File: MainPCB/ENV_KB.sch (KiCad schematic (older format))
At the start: 197 parts, among them J0 TYPE-C-31-M-12

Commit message: Changed Button to B3U from EVQ + smaller LED resistor
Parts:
- PowerLED0: value Green Power Led -> LED 0805
- PowerLedResistor0: value 1K Resistor -> 1K Resistor 0402; footprint Resistor_SMD:R_0805_2012Metric -> Resistor_SMD:R_0402_1005Metric
- RESISTOR0, RESISTOR1: value 5.1kohm -> 5.1kohm 0402
- SW-RST0: value Reset Buton -> B3U-1000; footprint Button_Switch_SMD:Panasonic_EVQPUJ_EVQPUA -> Button_Switch_SMD:SW_SPST_B3U-1000P; symbol Switch:SW_Push_Dual -> Switch:SW_Push
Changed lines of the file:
@@
 P 9950 8950
 F 0 "RESISTOR1" V 9754 8950 39  0001 C CNN
-F 1 "5.1kohm" V 10050 8950 30  0000 C CNN
+F 1 "5.1kohm 0402" V 10050 8950 30  0000 C CNN
 F 2 "Resistor_SMD:R_0402_1005Metric" H 9950 8950 50  0001 C CNN
 F 3 "~" H 9950 8950 50  0001 C CNN
@@
 P 8350 8650
 F 0 "RESISTOR0" V 8154 8650 39  0001 C CNN
-F 1 "5.1kohm" V 8245 8650 50  0001 C CNN
+F 1 "5.1kohm 0402" V 8245 8650 50  0001 C CNN
 F 2 "Resistor_SMD:R_0402_1005Metric" H 8350 8650 50  0001 C CNN
 F 3 "~" H 8350 8650 50  0001 C CNN
@@
 P 8300 9950
 F 0 "PowerLED0" H 8293 10167 50  0001 C CNN
-F 1 "Green Power Led" H 8300 10050 50  0000 C CNN
+F 1 "LED 0805" H 8300 10050 50  0000 C CNN
 F 2 "LED_SMD:LED_0805_2012Metric_Castellated" H 8300 9950 50  0001 C CNN
 F 3 "~" H 8300 9950 50  0001 C CNN
@@
 P 8550 9950
 F 0 "PowerLedResistor0" V 8650 10200 50  0000 C CNN
-F 1 "1K Resistor" V 8700 10000 50  0001 C CNN
-F 2 "Resistor_SMD:R_0805_2012Metric" H 8550 9950 50  0001 C CNN
+F 1 "1K Resistor 0402" V 8700 10000 50  0001 C CNN
+F 2 "Resistor_SMD:R_0402_1005Metric" H 8550 9950 50  0001 C CNN
 F 3 "~" H 8550 9950 50  0001 C CNN
 F 4 "C17513" V 8550 9950 50  0001 C CNN "LSCS Part"
@@
 Resetbtn
 $Comp
-L Switch:SW_Push_Dual SW-RST0
+L Switch:SW_Push SW-RST0
 U 1 1 605FBFA6
 P 8550 10700
 F 0 "SW-RST0" H 8550 11100 50  0000 C CNN
-F 1 "Reset Buton" H 8550 10950 50  0000 C CNN
-F 2 "Button_Switch_SMD:Panasonic_EVQPUJ_EVQPUA" H 8550 10700 50  0001 L BNN
+F 1 "B3U-1000" H 8550 10950 50  0000 C CNN
+F 2 "Button_Switch_SMD:SW_SPST_B3U-1000P" H 8550 10700 50  0001 L BNN
 F 3 "" H 8550 10700 50  0001 L BNN
 F 4 "Omron" H 8550 10700 50  0001 L BNN "MANUFACTURER"
@@
 Text GLabel 8750 10700 2    50   Input ~ 0
 GND
-Text GLabel 8750 10900 2    50   Input ~ 0
-GND
-Text GLabel 8350 10900 0    50   Input ~ 0
-Resetbtn
 $Comp
 L Mechanical:MountingHole H7

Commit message: Re aligned all diodes and re-did traces for all diodes
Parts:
- removed H8: MountingHole, MountingHole:MountingHole_3.2mm_M3, symbol Mechanical:MountingHole
- D0, D1, D10, D11, D12, D13, D14, D15, D16, D17, D18, D19, D2, D20, D21, D22, D23, D24, D25, D26, D27, D28, D29, D3, D30, D31, D32, D33, D34, D35, D36, D37, D38, D39, D4, D40, D41, D42, D43, D44, D45, D46, D47, D48, D49, D5, D50, D51, D52, D53, D54, D55, D56, D57, D58, D59, D6, D60, D61, D62, D63, D64, D65, D66, D67, D68, D69, D7, D70, D71, D72, D73, D74, D75, D76, D77, D78, D79, D8, D80, D81, D82, D83, D84, D85, D86, D87, D88, D9: footprint CFTKB Bits:D_DO-35_SOD27_P5.08mm_Horizontal -> Diode_THT:D_DO-35_SOD27_P7.62mm_Horizontal
- J0: LCSC (none) -> C165948; LSCS Part C165948 -> (none)
- PowerLED0: value LED 0805 -> LED 0402; footprint LED_SMD:LED_0805_2012Metric_Castellated -> LED_SMD:LED_0402_1005Metric; LSCS Part C2297 -> (none)
- PowerLedResistor0: LCSC (none) -> C17513; LSCS Part C17513 -> (none)
- RESISTOR0, RESISTOR1: LCSC (none) -> C25905; LSCS Part C25905 -> (none)
- SW-RST0: LCSC (none) -> C231329

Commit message: changed type-c port and re-did some bits
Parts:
- removed J0: TYPE-C-31-M-12, EM_Extras:USB_C_Receptacle_HRO_TYPE-C-31-M-12, symbol Type-C-Lib:TYPE-C-31-M-12
- added USB1: HRO-TYPE-C-31-M-12, HRO-TYPE-C31-M-12:HRO-TYPE-C-31-M-12, symbol Type-C:HRO-TYPE-C-31-M-12
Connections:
- net labels added: VBUS
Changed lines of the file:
@@
 Text GLabel 12950 8900 1    50   Input ~ 0
 USB2_N
-Text GLabel 8450 8850 0    50   Input ~ 0
+Text GLabel 9300 8700 1    50   Input ~ 0
 USB2_N
-Text GLabel 9850 8850 2    50   Input ~ 0
+Text GLabel 9400 8700 1    50   Input ~ 0
 USB2_P
 Text GLabel 13100 8900 1    50   Input ~ 0
@@
 Text GLabel 13650 9100 2    50   Input ~ 0
 USBVBUS
-Text GLabel 9850 8450 2    50   Input ~ 0
+Text GLabel 8800 8700 1    50   Input ~ 0
 USBVBUS
-Text GLabel 10050 8950 2    50   Input ~ 0
+Text GLabel 9000 8500 1    50   Input ~ 0
 GND
 Text GLabel 12150 9300 0    50   Input ~ 0
@@
 L Device:R_Small RESISTOR1
 U 1 1 606333E5
-P 9950 8950
-F 0 "RESISTOR1" V 9754 8950 39  0001 C CNN
-F 1 "5.1kohm 0402" V 10050 8950 30  0000 C CNN
-F 2 "Resistor_SMD:R_0402_1005Metric" H 9950 8950 50  0001 C CNN
-F 3 "~" H 9950 8950 50  0001 C CNN
-F 4 "C25905" V 9950 8950 50  0001 C CNN "LCSC"
-	1    9950 8950
-	0    1    1    0
+P 9000 8600
+F 0 "RESISTOR1" V 8804 8600 39  0001 C CNN
+F 1 "5.1kohm 0402" V 9000 8700 30  0001 C CNN
+F 2 "Resistor_SMD:R_0402_1005Metric" H 9000 8600 50  0001 C CNN
+F 3 "~" H 9000 8600 50  0001 C CNN
+F 4 "C25905" V 9000 8600 50  0001 C CNN "LCSC"
+	1    9000 8600
+	1    0    0    -1
 $EndComp
 $Comp
 L Device:R_Small RESISTOR0
 U 1 1 6066AF89
-P 8350 8650
-F 0 "RESISTOR0" V 8154 8650 39  0001 C CNN
-F 1 "5.1kohm 0402" V 8245 8650 50  0001 C CNN
-F 2 "Resistor_SMD:R_0402_1005Metric" H 8350 8650 50  0001 C CNN
-F 3 "~" H 8350 8650 50  0001 C CNN
-F 4 "C25905" V 8350 8650 50  0001 C CNN "LCSC"
-	1    8350 8650
-	0    -1   -1   0
-$EndComp
-Text GLabel 8250 8650 0    50   Input ~ 0
-GND
-Text GLabel 9850 9150 2    50   Input ~ 0
-GND
-Text GLabel 9850 9250 2    50   Input ~ 0
-GND
-Text GLabel 9850 8750 2    50   Input ~ 0
+P 9600 8600
+F 0 "RESISTOR0" V 9404 8600 39  0001 C CNN
+F 1 "5.1kohm 0402" V 9495 8600 50  0001 C CNN
+F 2 "Resistor_SMD:R_0402_1005Metric" H 9600 8600 50  0001 C CNN
+F 3 "~" H 9600 8600 50  0001 C CNN
+F 4 "C25905" V 9600 8600 50  0001 C CNN "LCSC"
+	1    9600 8600
+	-1   0    0    1
+$EndComp
+Text GLabel 9600 8500 1    50   Input ~ 0
+GND
+Text GLabel 9800 8700 1    50   Input ~ 0
+GND
+Text GLabel 9900 8700 1    50   Input ~ 0
+GND
+Text GLabel 9100 8700 1    50   Input ~ 0
 USB2_N
-Text GLabel 8450 8750 0    50   Input ~ 0
+Text GLabel 9200 8700 1    50   Input ~ 0
 USB2_P
 $Comp
@@
 	0    1    1    0
 $EndComp
-$Comp
-L Type-C-Lib:TYPE-C-31-M-12 J0
-U 1 1 607F5ECC
-P 9150 8850
-F 0 "J0" H 9150 9517 50  0000 C CNN
-F 1 "TYPE-C-31-M-12" H 9150 9426 50  0000 C CNN
-F 2 "EM_Extras:USB_C_Receptacle_HRO_TYPE-C-31-M-12" H 9150 8250 50  0000 C CNN
-F 3 "~" H 9300 8850 50  0001 C CNN
-F 4 "HRO Electronics" H 9150 8850 50  0001 C CNN "MANUFACTURER"
-F 5 "3.31mm" H 9150 8850 50  0001 C CNN "MAXIMUM_PACKAGE_HEIGHT"
-F 6 "A" H 9150 8850 50  0001 C CNN "PARTREV"
-F 7 "Manufacturer Recommendations" H 9150 8850 50  0001 C CNN "STANDARD"
-F 8 "C165948" H 9150 8850 50  0001 C CNN "LCSC"
-	1    9150 8850
-	1    0    0    -1
-$EndComp
-Text GLabel 9850 9350 2    50   Input ~ 0
+Text GLabel 8700 8700 1    50   Input ~ 0
 GND
 $Comp
@@
 	1    0    0    -1
 $EndComp
+$Comp
+L Type-C:HRO-TYPE-C-31-M-12 USB1
+U 1 1 60AC4D40
+P 9250 8800
+F 0 "USB1" V 8650 9250 60  0000 C CNN
+F 1 "HRO-TYPE-C-31-M-12" V 8750 8800 60  0000 C CNN
+F 2 "HRO-TYPE-C31-M-12:HRO-TYPE-C-31-M-12" H 9250 8800 60  0001 C CNN
+F 3 "" H 9250 8800 60  0001 C CNN
+F 4 "C165948" H 9250 8800 50  0001 C CNN "LCSC"
+	1    9250 8800
+	0    -1   -1   0
+$EndComp
+Text GLabel 9700 8700 1    50   Input ~ 0
+VBUS
 $EndSCHEMATC

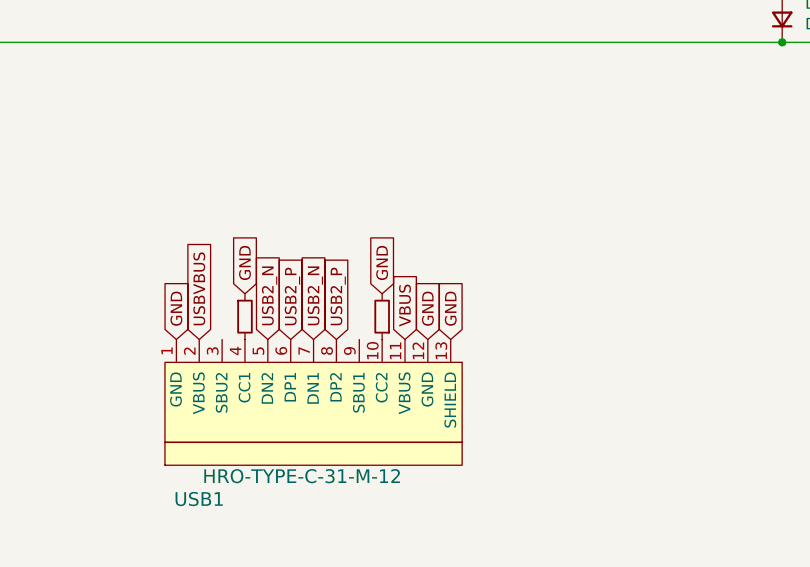
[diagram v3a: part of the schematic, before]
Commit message: adjusted traces, placements and clearances on main PCB and re-generated Gerber, Bom and Position file
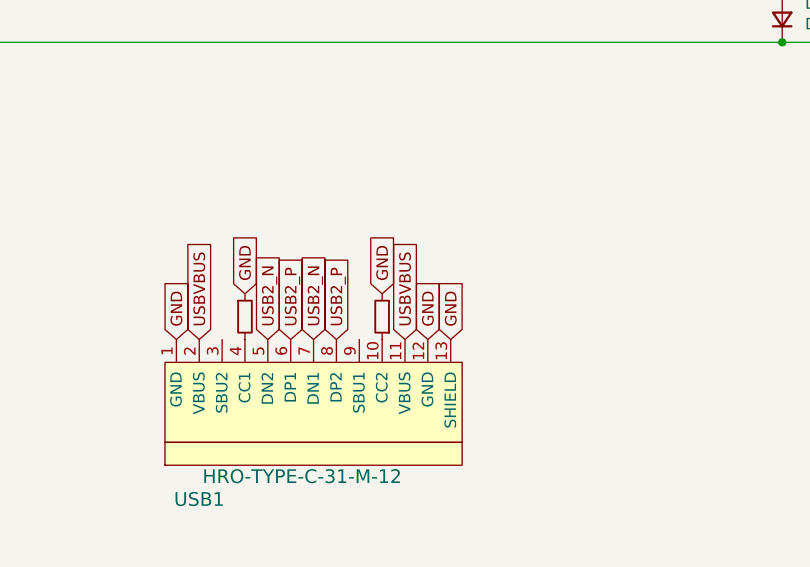
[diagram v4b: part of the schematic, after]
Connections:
- net VBUS is gone; now on net USBVBUS: USB1.11 (VBUS)
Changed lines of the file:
@@
 $EndComp
 Text GLabel 9700 8700 1    50   Input ~ 0
-VBUS
+USBVBUS
 $EndSCHEMATC

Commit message: some small alignment tweaks and corrections
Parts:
- K_0, K_1, K_10, K_11, K_12, K_13, K_14, K_15, K_16, K_17, K_18, K_19, K_2, K_20, K_21, K_22, K_23, K_24, K_25, K_26, K_27, K_28, K_3, K_30, K_31, K_32, K_34, K_35, K_36, K_37, K_38, K_39, K_4, K_40, K_41, K_42, K_43, K_44, K_45, K_47, K_48, K_49, K_5, K_51, K_52, K_53, K_54, K_55, K_56, K_57, K_58, K_59, K_6, K_60, K_61, K_62, K_65, K_66, K_67, K_68, K_69, K_7, K_70, K_71, K_72, K_73, K_74, K_75, K_77, K_8, K_86, K_87, K_88, K_9: footprint MX_only:MXOnly-1U-NoLED -> MX_Only:MXOnly-1U-NoLED
- K_29: footprint MX_only:MXOnly-2U-NoLED -> MX_Only:MXOnly-2U-NoLED
- K_33, K_46: footprint MX_only:MXOnly-1.5U-NoLED -> MX_Only:MXOnly-1.5U-NoLED
- K_50: footprint MX_only:MXOnly-1.75U-NoLED -> MX_Only:MXOnly-1.75U-NoLED
- K_63B1, K_64B1: footprint MX_only:MXOnly-2.25U-NoLED -> MX_Only:MXOnly-2.25U-NoLED
- K_64, K_78, K_79, K_80, K_82, K_83, K_84, K_85: footprint MX_only:MXOnly-1.25U-NoLED -> MX_Only:MXOnly-1.25U-NoLED
- K_76: footprint MX_only:MXOnly-2.75U-NoLED -> MX_Only:MXOnly-2.75U-NoLED
- K_81: footprint MX_only:MXOnly-6.25U-ReversedStabilizers-NoLED -> MX_Only:MXOnly-6.25U-ReversedStabilizers-NoLED

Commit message: increased Resistor value for led as it was too bright.
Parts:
- PowerLedResistor0: value 1K Resistor 0402 -> 2K Resistor 0402
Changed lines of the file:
@@
 P 8550 9950
 F 0 "PowerLedResistor0" V 8650 10200 50  0000 C CNN
-F 1 "1K Resistor 0402" V 8700 10000 50  0001 C CNN
+F 1 "2K Resistor 0402" V 8700 10000 50  0001 C CNN
 F 2 "Resistor_SMD:R_0402_1005Metric" H 8550 9950 50  0001 C CNN
 F 3 "~" H 8550 9950 50  0001 C CNN

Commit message: Corrected a mistake in the silkscreen, overlapping a contributor initials and footprint
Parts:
- PowerLedResistor0: value 2K Resistor 0402 -> 2.2K Resistor 0402
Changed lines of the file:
@@
 P 8550 9950
 F 0 "PowerLedResistor0" V 8650 10200 50  0000 C CNN
-F 1 "2K Resistor 0402" V 8700 10000 50  0001 C CNN
+F 1 "2.2K Resistor 0402" V 8700 10000 50  0001 C CNN
 F 2 "Resistor_SMD:R_0402_1005Metric" H 8550 9950 50  0001 C CNN
 F 3 "~" H 8550 9950 50  0001 C CNN

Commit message: Changed all mount holes to M2 and added some pads around the holes to avoid scratches being visible on pcbs
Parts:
- H0, H1, H10, H3, H4, H6, H7, H9: footprint MountingHole:MountingHole_3.2mm_M3 -> MountingHole:MountingHole_2.2mm_M2_Pad
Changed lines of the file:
@@
 F 0 "H9" H 6700 10696 50  0000 L CNN
 F 1 "MountingHole" H 6700 10605 50  0000 L CNN
-F 2 "MountingHole:MountingHole_3.2mm_M3" H 6600 10650 50  0001 C CNN
+F 2 "MountingHole:MountingHole_2.2mm_M2_Pad" H 6600 10650 50  0001 C CNN
 F 3 "~" H 6600 10650 50  0001 C CNN
 	1    6600 10650
@@
 F 0 "H10" H 6700 10896 50  0000 L CNN
 F 1 "MountingHole" H 6700 10805 50  0000 L CNN
-F 2 "MountingHole:MountingHole_3.2mm_M3" H 6600 10850 50  0001 C CNN
+F 2 "MountingHole:MountingHole_2.2mm_M2_Pad" H 6600 10850 50  0001 C CNN
 F 3 "~" H 6600 10850 50  0001 C CNN
 	1    6600 10850
@@
 F 0 "H7" H 6700 10296 50  0000 L CNN
 F 1 "MountingHole" H 6700 10205 50  0000 L CNN
-F 2 "MountingHole:MountingHole_3.2mm_M3" H 6600 10250 50  0001 C CNN
+F 2 "MountingHole:MountingHole_2.2mm_M2_Pad" H 6600 10250 50  0001 C CNN
 F 3 "~" H 6600 10250 50  0001 C CNN
 	1    6600 10250
@@
 F 0 "H6" H 6700 10096 50  0000 L CNN
 F 1 "MountingHole" H 6700 10005 50  0000 L CNN
-F 2 "MountingHole:MountingHole_3.2mm_M3" H 6600 10050 50  0001 C CNN
+F 2 "MountingHole:MountingHole_2.2mm_M2_Pad" H 6600 10050 50  0001 C CNN
 F 3 "~" H 6600 10050 50  0001 C CNN
 	1    6600 10050
@@
 F 0 "H4" H 6700 9696 50  0000 L CNN
 F 1 "MountingHole" H 6700 9605 50  0000 L CNN
-F 2 "MountingHole:MountingHole_3.2mm_M3" H 6600 9650 50  0001 C CNN
+F 2 "MountingHole:MountingHole_2.2mm_M2_Pad" H 6600 9650 50  0001 C CNN
 F 3 "~" H 6600 9650 50  0001 C CNN
 	1    6600 9650
@@
 F 0 "H1" H 6700 9096 50  0000 L CNN
 F 1 "MountingHole" H 6700 9005 50  0000 L CNN
-F 2 "MountingHole:MountingHole_3.2mm_M3" H 6600 9050 50  0001 C CNN
+F 2 "MountingHole:MountingHole_2.2mm_M2_Pad" H 6600 9050 50  0001 C CNN
 F 3 "~" H 6600 9050 50  0001 C CNN
 	1    6600 9050
@@
 F 0 "H3" H 6700 9496 50  0000 L CNN
 F 1 "MountingHole" H 6700 9405 50  0000 L CNN
-F 2 "MountingHole:MountingHole_3.2mm_M3" H 6600 9450 50  0001 C CNN
+F 2 "MountingHole:MountingHole_2.2mm_M2_Pad" H 6600 9450 50  0001 C CNN
 F 3 "~" H 6600 9450 50  0001 C CNN
 	1    6600 9450
@@
 F 0 "H0" H 6700 8896 50  0000 L CNN
 F 1 "MountingHole" H 6700 8805 50  0000 L CNN
-F 2 "MountingHole:MountingHole_3.2mm_M3" H 6600 8850 50  0001 C CNN
+F 2 "MountingHole:MountingHole_2.2mm_M2_Pad" H 6600 8850 50  0001 C CNN
 F 3 "~" H 6600 8850 50  0001 C CNN
 	1    6600 8850
